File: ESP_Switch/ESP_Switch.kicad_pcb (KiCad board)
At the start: 2 copper layers, 47.8 x 27.7 mm, 30 parts, among them J1 Boot, J2 PRGM, J3 IO, J5 Expansion, J6 EXP2, J7 0548190519, U1 ESP-12E, U2 AMS1117-3.3

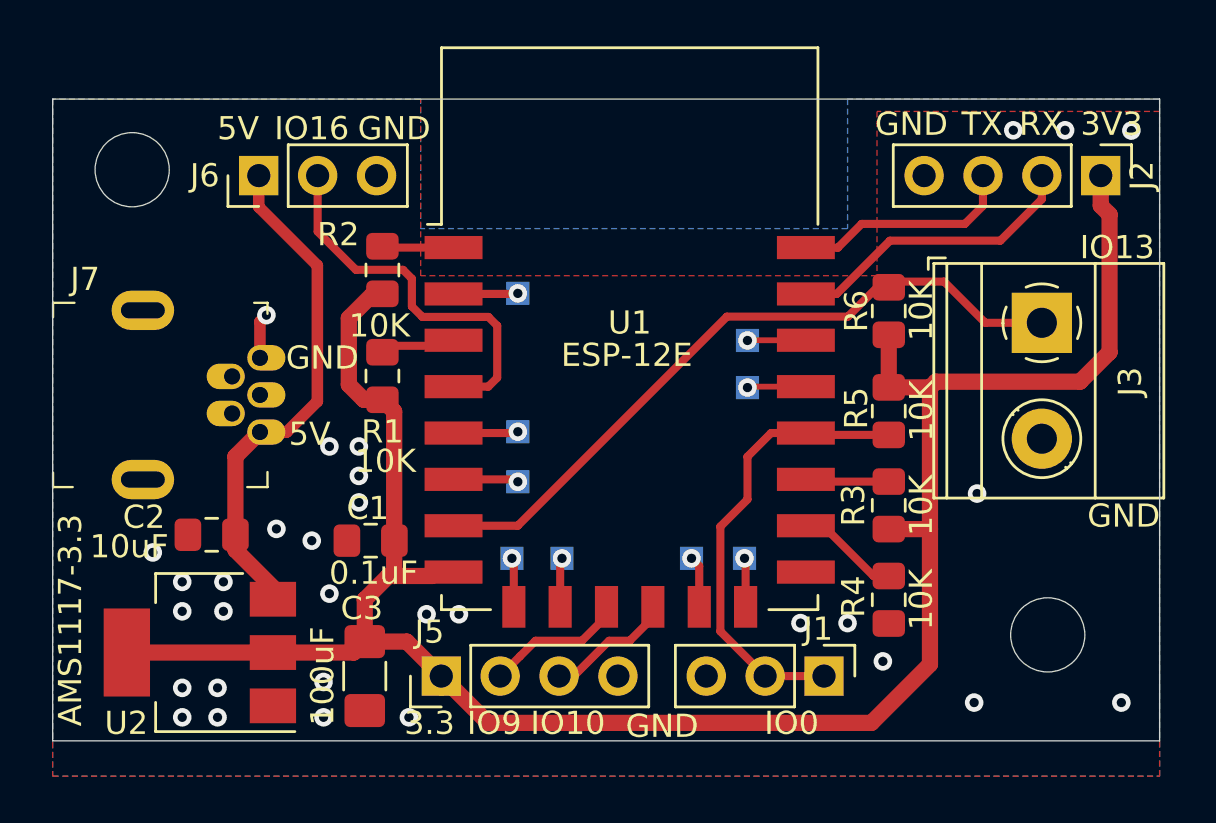
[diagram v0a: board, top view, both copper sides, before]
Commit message: added power distros
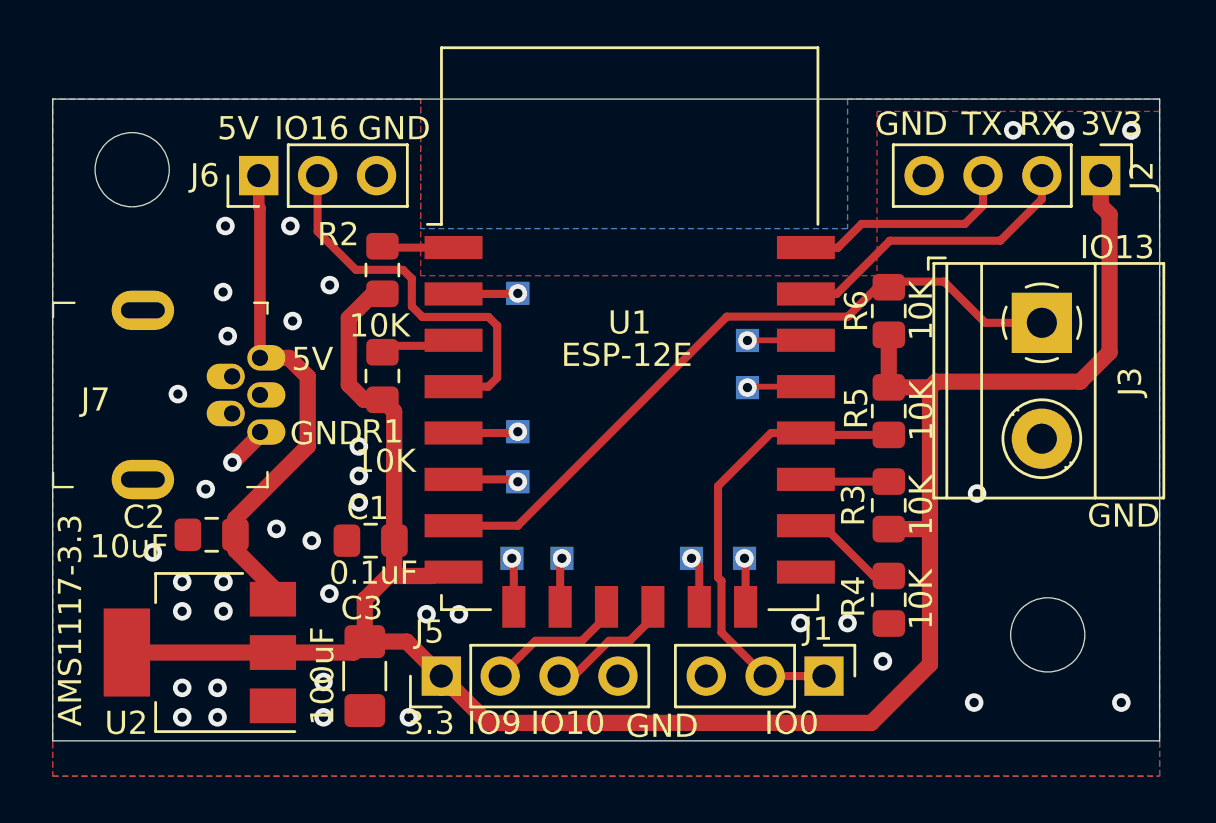
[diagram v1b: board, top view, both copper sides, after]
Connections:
- J7 pad 1: +5V -> GND
- J7 pad 5: GND -> +5V
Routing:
- net GND: track 1.96 -> 1.80 mm, vias 31 -> 38
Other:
- net class Power: trace_width 0.5 -> 0.7
- board text added: "ESP Switch v1.2"
- board text removed: "ESP Switch v1.1"
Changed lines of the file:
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@@
     (thickness 1.6)
     (drawings 47)
-    (tracks 172)
+    (tracks 180)
     (zones 0)
     (modules 30)
@@
   (title_block
     (title "ESP Switch")
-    (date 2020-04-12)
-    (rev v1.1)
+    (date 2020-06-10)
+    (rev v1.2)
   )
   (layers
@@
   (net_class Power ""
     (clearance 0.1)
-    (trace_width 0.5)
+    (trace_width 0.7)
     (via_dia 0.8)
     (via_drill 0.4)
@@
   (module digikey-footprints:USB_Mini_B_Female_548190519 (layer F.Cu)
     (at 88.1888 90.4875)
-    (fp_text reference J7 (at -7.5438 -4.9911) (layer F.SilkS)
+    (fp_text reference J7 (at -7.0888 0.2125) (layer F.SilkS)
       (effects (font (size 1 1) (thickness 0.15)))
     )
@@
       (net 13 "Net-(J7-Pad4)"))
     (pad 1 thru_hole oval (at 0 1.6) (size 1.65 1.1) (drill 0.7 (offset 0.275 0)) (layers *.Cu *.Mask)
+      (net 1 GND))
+    (pad 5 thru_hole oval (at 0 -1.6) (size 1.65 1.1) (drill 0.7 (offset 0.275 0)) (layers *.Cu *.Mask)
       (net 3 +5V))
-    (pad 5 thru_hole oval (at 0 -1.6) (size 1.65 1.1) (drill 0.7 (offset 0.275 0)) (layers *.Cu *.Mask)
-      (net 1 GND))
     (pad 3 thru_hole oval (at 0 0) (size 1.65 1.1) (drill 0.7 (offset 0.275 0)) (layers *.Cu *.Mask)
       (net 12 "Net-(J7-Pad3)"))
@@
     )
   )
-  (gr_text GND (at 90.8812 88.8873) (layer F.SilkS)
+  (gr_text GND (at 91.05 92.15) (layer F.SilkS)
     (effects (font (size 1 1) (thickness 0.15)))
   )
-  (gr_text 5V (at 90.3351 92.1766) (layer F.SilkS)
+  (gr_text 5V (at 90.45 88.95) (layer F.SilkS)
     (effects (font (size 1 1) (thickness 0.15)))
   )
@@
     (effects (font (size 1 1) (thickness 0.15)) (justify mirror))
   )
-  (gr_text 5V (at 90.3605 92.1766) (layer B.SilkS)
-    (effects (font (size 1 1) (thickness 0.15)) (justify mirror))
-  )
-  (gr_text GND (at 90.8939 88.9127) (layer B.SilkS)
-    (effects (font (size 1 1) (thickness 0.15)) (justify mirror))
-  )
-  (gr_text "ESP Switch v1.1" (at 103.886 79.121) (layer B.SilkS)
+  (gr_text 5V (at 90.55 88.95) (layer B.SilkS)
+    (effects (font (size 1 1) (thickness 0.15)) (justify mirror))
+  )
+  (gr_text GND (at 91.05 92.15) (layer B.SilkS)
+    (effects (font (size 1 1) (thickness 0.15)) (justify mirror))
+  )
+  (gr_text "ESP Switch v1.2" (at 103.886 79.121) (layer B.SilkS)
     (effects (font (size 1 1) (thickness 0.15)) (justify mirror))
   )
@@
   (via (at 92.456 92.71) (size 0.8) (drill 0.4) (layers F.Cu B.Cu) (net 1))
   (via (at 92.456 93.98) (size 0.8) (drill 0.4) (layers F.Cu B.Cu) (net 1))
-  (via (at 91.186 92.71) (size 0.8) (drill 0.4) (layers F.Cu B.Cu) (net 1))
   (via (at 92.456 95.123) (size 0.8) (drill 0.4) (layers F.Cu B.Cu) (net 1))
   (via (at 125.7808 79.0829) (size 0.8) (drill 0.4) (layers F.Cu B.Cu) (net 1))
@@
   (via (at 118.999 103.759) (size 0.8) (drill 0.4) (layers F.Cu B.Cu) (net 1))
   (via (at 125.349 103.759) (size 0.8) (drill 0.4) (layers F.Cu B.Cu) (net 1))
-  (via (at 88.4682 87.0458) (size 0.8) (drill 0.4) (layers F.Cu B.Cu) (net 1))
-  (segment (start 88.1888 87.3252) (end 88.4682 87.0458) (width 0.5) (layer F.Cu) (net 1))
-  (segment (start 88.1888 88.8875) (end 88.1888 87.3252) (width 0.5) (layer F.Cu) (net 1))
+  (via (at 86.6 86.05) (size 0.8) (drill 0.4) (layers F.Cu B.Cu) (net 1))
+  (via (at 86.7 83.2) (size 0.8) (drill 0.4) (layers F.Cu B.Cu) (net 1))
+  (via (at 89.5 83.2) (size 0.8) (drill 0.4) (layers F.Cu B.Cu) (net 1))
+  (via (at 91.2 85.75) (size 0.8) (drill 0.4) (layers F.Cu B.Cu) (net 1))
+  (via (at 89.6 87.3) (size 0.8) (drill 0.4) (layers F.Cu B.Cu) (net 1))
+  (via (at 87 93.4) (size 0.8) (drill 0.4) (layers F.Cu B.Cu) (net 1))
+  (via (at 86.8 87.95) (size 0.8) (drill 0.4) (layers F.Cu B.Cu) (net 1))
+  (segment (start 88.1888 92.2112) (end 87 93.4) (width 0.7) (layer F.Cu) (net 1))
+  (segment (start 88.1888 92.0875) (end 88.1888 92.2112) (width 0.7) (layer F.Cu) (net 1))
+  (via (at 84.65 90.45) (size 0.8) (drill 0.4) (layers F.Cu B.Cu) (net 1))
+  (via (at 85.85 94.55) (size 0.8) (drill 0.4) (layers F.Cu B.Cu) (net 1))
   (segment (start 115.325 96.266) (end 115.316 96.275) (width 0.7) (layer F.Cu) (net 2))
   (segment (start 117.085 90.161) (end 115.316 90.161) (width 0.7) (layer F.Cu) (net 2))
@@
   (segment (start 87.131 97.175) (end 89.256 99.3) (width 0.7) (layer F.Cu) (net 3))
   (segment (start 87.131 96.52) (end 87.131 97.175) (width 0.7) (layer F.Cu) (net 3))
-  (segment (start 87.131 93.1453) (end 88.1888 92.0875) (width 0.7) (layer F.Cu) (net 3))
-  (segment (start 87.131 96.52) (end 87.131 93.1453) (width 0.7) (layer F.Cu) (net 3))
   (segment (start 88.138 82.376) (end 88.138 81.026) (width 0.5) (layer F.Cu) (net 3))
-  (segment (start 90.6653 84.9033) (end 88.138 82.376) (width 0.5) (layer F.Cu) (net 3))
-  (segment (start 90.6653 90.7669) (end 90.6653 84.9033) (width 0.5) (layer F.Cu) (net 3))
-  (segment (start 88.1888 92.0875) (end 89.3447 92.0875) (width 0.5) (layer F.Cu) (net 3))
-  (segment (start 89.3447 92.0875) (end 90.6653 90.7669) (width 0.5) (layer F.Cu) (net 3))
+  (segment (start 88.1888 88.8875) (end 88.1888 82.4268) (width 0.5) (layer F.Cu) (net 3))
+  (segment (start 88.1888 82.4268) (end 88.138 82.376) (width 0.5) (layer F.Cu) (net 3))
+  (segment (start 87.131 95.819) (end 87.131 96.52) (width 0.7) (layer F.Cu) (net 3))
+  (segment (start 90.25 92.7) (end 87.131 95.819) (width 0.7) (layer F.Cu) (net 3))
+  (segment (start 90.25 89.7) (end 90.25 92.7) (width 0.7) (layer F.Cu) (net 3))
+  (segment (start 88.1888 88.8875) (end 89.4375 88.8875) (width 0.7) (layer F.Cu) (net 3))
+  (segment (start 89.4375 88.8875) (end 90.25 89.7) (width 0.7) (layer F.Cu) (net 3))
   (segment (start 119.479004 87.376) (end 121.92 87.376) (width 0.35) (layer F.Cu) (net 4))
   (segment (start 117.701004 85.598) (end 119.479004 87.376) (width 0.35) (layer F.Cu) (net 4))
@@
   (segment (start 113.5507 87.1093) (end 115.071 85.589) (width 0.35) (layer F.Cu) (net 4))
   (segment (start 115.071 85.589) (end 115.316 85.589) (width 0.35) (layer F.Cu) (net 4))
-  (segment (start 111.74 86.13) (end 110.99 86.13) (width 0.25) (layer F.Cu) (net 26))
   (segment (start 101.092 102.362) (end 101.092 102.87) (width 0.25) (layer F.Cu) (net 5))
   (segment (start 105.14 99.63) (end 105.14 100.03) (width 0.25) (layer F.Cu) (net 5))
@@
   (segment (start 115.316 92.211) (end 111.821 92.211) (width 0.35) (layer F.Cu) (net 11))
   (segment (start 112.522 102.616) (end 109.982 102.616) (width 0.35) (layer F.Cu) (net 11))
+  (segment (start 108.1 100.734) (end 108.1 98.514998) (width 0.35) (layer F.Cu) (net 11))
+  (segment (start 107.95 94.42) (end 110.24 92.13) (width 0.35) (layer F.Cu) (net 11))
   (segment (start 110.24 92.13) (end 111.74 92.13) (width 0.35) (layer F.Cu) (net 11))
-  (segment (start 108.0516 100.6856) (end 108.0516 96.1644) (width 0.35) (layer F.Cu) (net 11))
-  (segment (start 109.982 102.616) (end 108.0516 100.6856) (width 0.35) (layer F.Cu) (net 11))
-  (segment (start 108.0516 96.1644) (end 109.22 94.996) (width 0.35) (layer F.Cu) (net 11))
-  (segment (start 109.22 94.996) (end 109.22 93.15) (width 0.35) (layer F.Cu) (net 11))
-  (segment (start 109.22 93.15) (end 110.24 92.13) (width 0.35) (layer F.Cu) (net 11))
+  (segment (start 109.982 102.616) (end 108.1 100.734) (width 0.35) (layer F.Cu) (net 11))
+  (segment (start 108.1 98.514998) (end 107.95 98.364998) (width 0.35) (layer F.Cu) (net 11))
+  (segment (start 107.95 98.364998) (end 107.95 94.42) (width 0.35) (layer F.Cu) (net 11))
   (segment (start 90.678 83.439) (end 90.678 81.026) (width 0.35) (layer F.Cu) (net 15))
   (segment (start 94.361 85.09) (end 92.329 85.09) (width 0.35) (layer F.Cu) (net 15))
@@
   (segment (start 119.38 82.32775) (end 119.38 81.026) (width 0.35) (layer F.Cu) (net 25))
   (segment (start 118.59895 83.1088) (end 119.38 82.32775) (width 0.35) (layer F.Cu) (net 25))
+  (segment (start 111.74 86.13) (end 110.99 86.13) (width 0.25) (layer F.Cu) (net 26))
   (segment (start 115.3668 83.8327) (end 120.1293 83.8327) (width 0.35) (layer F.Cu) (net 26))
   (segment (start 121.92 82.042) (end 121.92 81.026) (width 0.35) (layer F.Cu) (net 26))

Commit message: Added Pic and readme
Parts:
- moved J3 5.03 mm to (122.2, 92.4), turned to 90 degrees
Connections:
- J3 pad 1: /GPIO13 -> GND
- J3 pad 2: GND -> /GPIO13
